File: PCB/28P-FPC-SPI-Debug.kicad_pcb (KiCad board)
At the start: 2 copper layers, 35.5 x 40 mm, 20 parts, among them J1 Conn_01x24, J3 SFV24R-1STBE1HLF, Q1 Si1308EDL

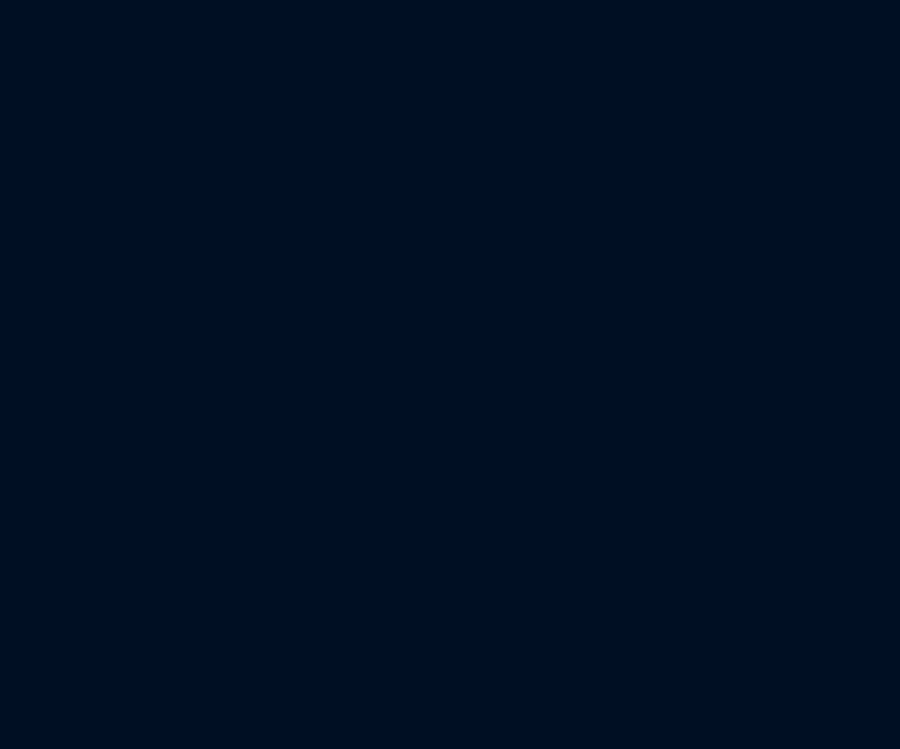
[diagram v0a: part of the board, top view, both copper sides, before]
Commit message: Modified power enable circuit to v2.2 ref design and added note.
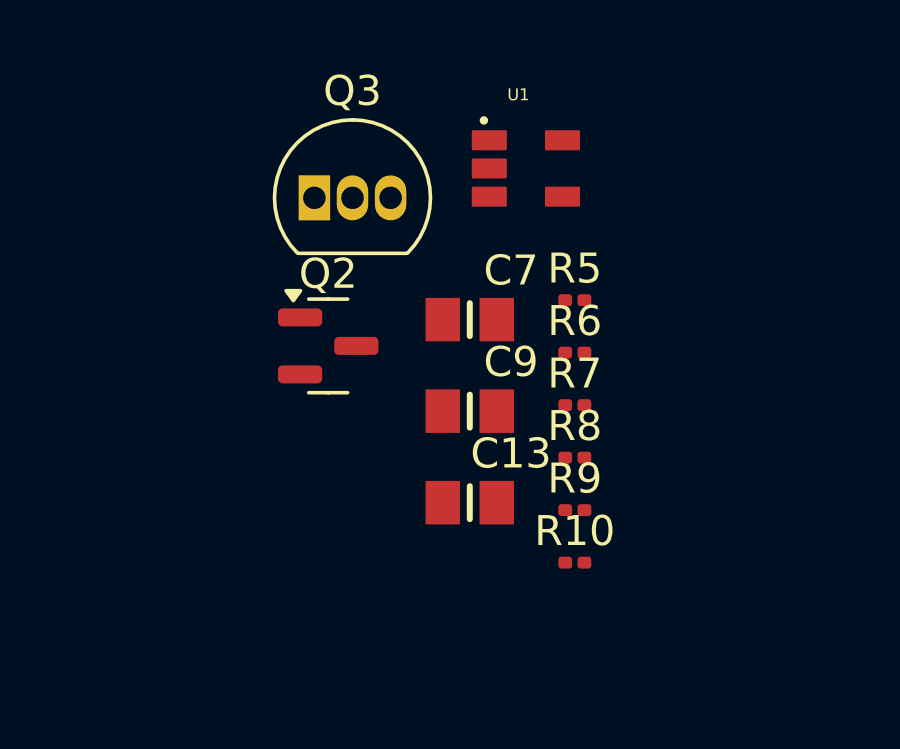
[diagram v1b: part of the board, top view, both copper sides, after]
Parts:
- added C13: 0.1u/50V, capacitors-cam:CAPC2012X140N, F.Cu at (96.2, 54.0)
- added C7: 1u/50V, capacitors-cam:CAPC2012X140N, F.Cu at (96.2, 47.9)
- added C9: 1u/50V, capacitors-cam:CAPC2012X140N, F.Cu at (96.2, 51.0)
- added Q2: AO3401A, Package_TO_SOT_SMD:SOT-23, F.Cu at (91.4, 48.8)
- added Q3: S8050, Package_TO_SOT_THT:TO-92_Inline, F.Cu at (91.0, 43.8)
- added R10: 100K, Resistor_SMD:R_0201_0603Metric, F.Cu at (99.7, 56.0)
- added R5: 1K, Resistor_SMD:R_0201_0603Metric, F.Cu at (99.7, 47.2)
- added R6: 47K, Resistor_SMD:R_0201_0603Metric, F.Cu at (99.7, 49.0)
- added R7: 47K, Resistor_SMD:R_0201_0603Metric, F.Cu at (99.7, 50.8)
- added R8: 1K, Resistor_SMD:R_0201_0603Metric, F.Cu at (99.7, 52.5)
- added R9: 47K, Resistor_SMD:R_0201_0603Metric, F.Cu at (99.7, 54.2)
- added U1: RT9193-33GB, VoltageRegulators:SOT94P279X129-5N, F.Cu at (98.0, 42.9)
- C3: value 1u/50V -> 0.1u/50V

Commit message: Added voltage level shifter TXB018PW
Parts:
- added J1: Conn_01x08, Connector_Samtec_HLE_THT:Samtec_HLE-104-02-xx-DV-TE_2x04_P2.54mm_Horizontal, F.Cu at (50.5, 47.9)
- moved R5 44.3 mm to (56.0, 54.5), turned to 180 degrees
- moved R8 43.8 mm to (56.0, 55.5)
- moved R7 43.2 mm to (56.6, 47.9), turned to 180 degrees
- moved R9 39.4 mm to (60.5, 59.0)
- moved R6 36.9 mm to (63.2, 54.5)
- moved Q2 30.1 mm to (63.0, 39.0)
- moved R10 28.4 mm to (71.3, 53.5)
- moved U1 25.0 mm to (75.0, 52.5)
- moved Q3 22.0 mm to (70.0, 37.5)
- moved C9 16.7 mm to (79.5, 49.5), turned to -90 degrees
- moved C13 14.9 mm to (82.0, 49.5), turned to -90 degrees
- moved Q1 13.0 mm to (128.5, 91.0)
- moved C7 11.8 mm to (84.5, 49.5), turned to -90 degrees
- moved L1 5.73 mm to (120.0, 82.5)
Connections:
- J3 pad 10: /RST -> /\RST
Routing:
- net Net-(Q3-B): track 0.00 -> 23.2 mm
- net Net-(U1-BP): track 0.00 -> 9.54 mm
- net /\RST: track 0.00 -> 6.62 mm
- net +3V3: track 0.00 -> 6.26 mm
- net /Vcc: track 0.00 -> 6.20 mm
- net /VCC_INT: track 0.00 -> 5.70 mm
- net GND: track 0.00 -> 3.29 mm
- net /VCC_EN: track 0.00 -> 2.14 mm
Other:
- board outline removed

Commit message: Added nets for TXB018PW. Resized PCB to size of 2.13in e-paper display with ~5mm excess on edges. Questionable part placement start.
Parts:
- removed the J1 at (93.0, 71.8)
- added C14: 1u/25V, capacitors-cam:CAPC1608X90N, F.Cu at (124.2, 29.5)
- added U2: TXB0108PW, Package_SO:TSSOP-20_4.4x6.5mm_P0.65mm, F.Cu at (163.0, 59.8)
- moved J1 145.3 mm to (195.0, 63.8), turned to 90 degrees
- moved R7 133.7 mm to (189.0, 66.0), turned to 0 degrees
- moved Q2 128.3 mm to (189.0, 63.0), turned to 90 degrees
- moved R5 126.7 mm to (182.3, 63.8), turned to 0 degrees
- moved R8 126.7 mm to (182.3, 64.8), turned to 180 degrees
- moved R9 124.0 mm to (184.3, 64.8), turned to 180 degrees
- moved Q3 123.9 mm to (188.6, 73.2), turned to 90 degrees
- moved R6 121.5 mm to (184.3, 63.8)
- moved R10 118.9 mm to (190.1, 57.8), turned to 90 degrees
- moved U1 114.2 mm to (189.1, 54.2), turned to 90 degrees
- moved C9 105.1 mm to (184.4, 55.4), turned to 0 degrees
- moved C13 102.4 mm to (184.4, 52.9), turned to 0 degrees
- moved C7 99.9 mm to (184.4, 50.4), turned to 0 degrees
- moved C12 76.3 mm to (179.6, 64.5), turned to -90 degrees
- moved J3 76.2 mm to (145.0, 60.0)
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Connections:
- J3 pad 10: /\RST -> /\EPD_RST
- J3 pad 11: /D/C -> /EPD_D/C
- J3 pad 12: /CS -> /EPD_CS
- J3 pad 13: /SCLK -> /EPD_SCLK
- J3 pad 14: /SDI -> /EPD_SDI
- J3 pad 9: /BUSY -> /EPD_BUSY
- R10 pad 1: GND -> /VCC_EN
- R10 pad 2: /VCC_EN -> GND
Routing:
- net Net-(Q3-B): track 23.2 -> 0.00 mm
- net Net-(Q2-G): track 0.00 -> 7.28 mm
- net /\RST: track 6.62 -> 0.00 mm
- net Net-(D2-A): track 0.00 -> 4.28 mm
- net Net-(D1-K): track 0.00 -> 4.20 mm
- net /Vcc: track 6.20 -> 9.92 mm
- net Net-(U1-BP): track 9.54 -> 5.84 mm
- net +3V3: track 6.26 -> 2.92 mm
- net /VDD: track 1.95 -> 0.00 mm
- net /VCC_INT: track 5.70 -> 7.59 mm
- net /D/C: track 1.07 -> 0.00 mm
- net /BUSY: track 1.07 -> 0.00 mm
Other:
- board outline added: 60 x 30 mm

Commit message: track placement, parts moved, nightmare fuel.
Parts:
- moved C14 49.8 mm to (167.0, 55.0), turned to 90 degrees
- moved C3 15.3 mm to (161.0, 69.4), turned to 90 degrees
- moved R5 12.3 mm to (191.2, 72.4), turned to -90 degrees
- moved C4 11.6 mm to (158.6, 69.4), turned to 90 degrees
- moved R8 11.1 mm to (190.0, 72.8)
- moved R6 9.96 mm to (190.0, 72.0)
- moved U2 9.44 mm to (172.3, 58.3)
- moved C5 8.83 mm to (156.6, 69.4), turned to 90 degrees
- moved R9 8.71 mm to (188.6, 72.4), turned to -90 degrees
- moved R2 7.45 mm to (172.3, 65.6), turned to 90 degrees
- moved D1 7.26 mm to (166.4, 72.2), turned to 180 degrees
- moved C2 6.91 mm to (153.0, 47.7), turned to -90 degrees
- moved C10 5.46 mm to (150.8, 69.4), turned to 90 degrees
- moved C1 4.86 mm to (151.0, 47.7), turned to -90 degrees
- moved R7 4.68 mm to (192.3, 62.6), turned to 90 degrees
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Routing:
- net /\RST: track 0.00 -> 43.5 mm, vias 0 -> 4
- net GND: track 3.29 -> 41.7 mm, vias 0 -> 7
- net /VCC_EN: track 2.14 -> 29.8 mm, vias 0 -> 3
- net /BUSY: track 0.00 -> 27.6 mm, vias 0 -> 2
- net +3V3: track 2.92 -> 27.4 mm, vias 0 -> 1
- net /SCLK: track 0.00 -> 24.3 mm, vias 0 -> 2
- net /D/C: track 0.00 -> 23.8 mm, vias 0 -> 2
- net /EPD_BUSY: track 0.00 -> 22.7 mm
- net /\EPD_RST: track 0.00 -> 22.6 mm
- net /EPD_D/C: track 0.00 -> 22.6 mm
- net /EPD_CS: track 0.00 -> 22.5 mm
- net /EPD_SCLK: track 0.00 -> 22.5 mm
- net /EPD_SDI: track 0.00 -> 22.4 mm
- net /SDI: track 0.00 -> 20.4 mm
- net /PREVGL: track 0.00 -> 20.2 mm, vias 0 -> 2
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
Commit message: track placement
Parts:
- moved R3 78.5 mm to (186.8, 49.4), turned to 90 degrees
- moved Q1 3.35 mm to (171.2, 64.8), turned to 90 degrees
- moved R2 2.10 mm to (173.2, 63.7)
- moved R1 2.07 mm to (168.2, 64.9)
- moved C11 2.01 mm to (170.4, 69.6)
- moved C12 1.05 mm to (179.4, 66.8)
- moved C6 0.22 mm to (154.4, 69.4)
- moved C8 0.22 mm to (152.8, 69.4)
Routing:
- net GND: track 41.7 -> 156.6 mm, vias 7 -> 14
- net +3V3: track 27.4 -> 91.5 mm, vias 1 -> 8
- net /GDR: track 2.03 -> 29.4 mm, vias 1 -> 3
- net /Vcc: track 16.6 -> 29.3 mm
- net Net-(D2-A): track 0.00 -> 11.7 mm
- net Net-(D1-K): track 0.00 -> 6.04 mm
- net /RESE: track 0.00 -> 2.08 mm

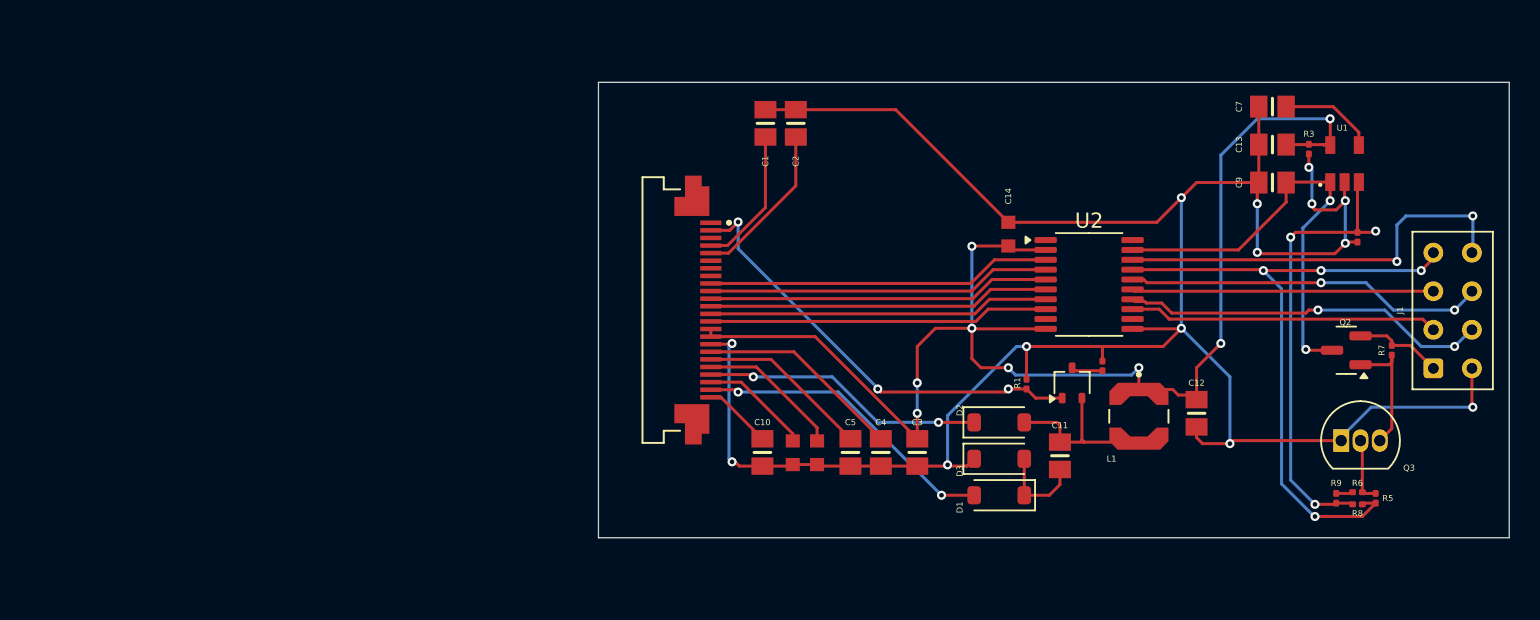
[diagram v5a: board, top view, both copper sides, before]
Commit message: Added breakout 28pin header for debugging. Track cleanup. Changed 0603 footprint due to clearance violations. Increased board size to fit header.
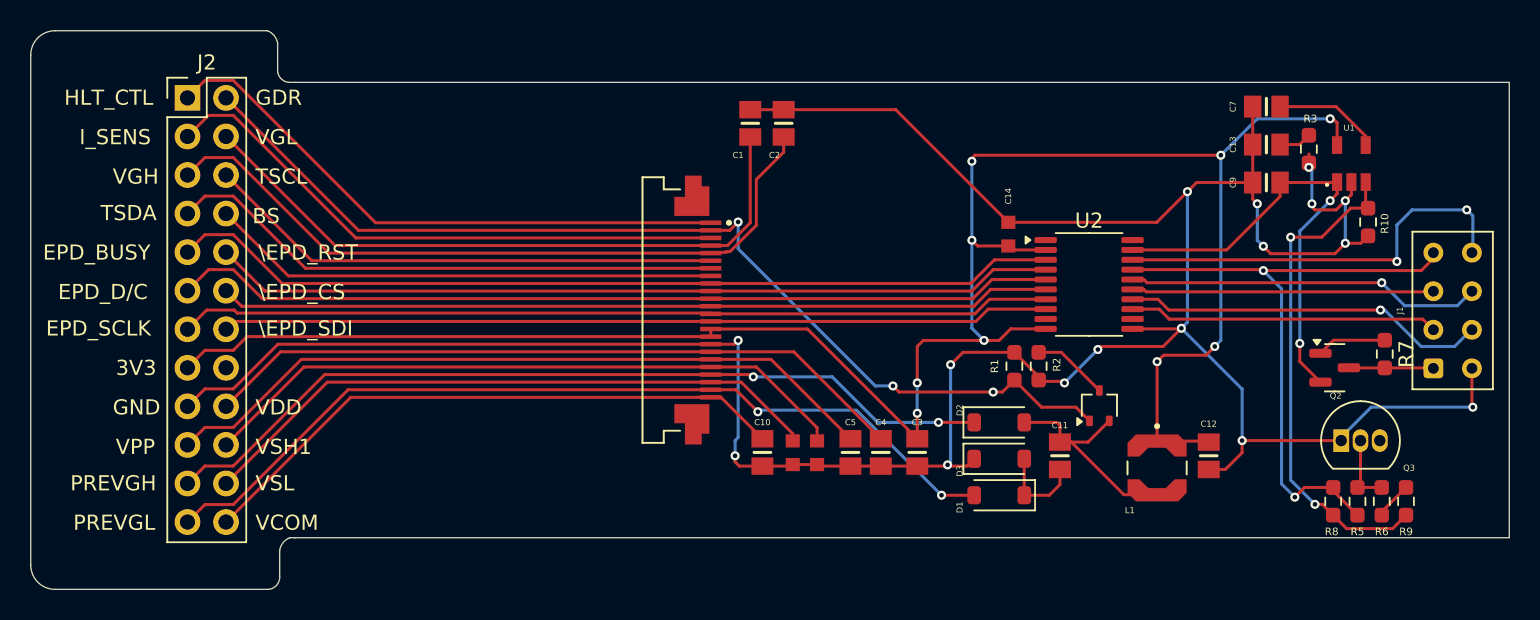
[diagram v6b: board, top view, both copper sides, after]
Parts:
- added J2: Conn_01x24, Connector_PinHeader_2.54mm:PinHeader_2x12_P2.54mm_Vertical, F.Cu at (112.9, 46.0)
- R1, R10, R2, R3, R6, R7, R8, R9: footprint Resistor_SMD:R_0201_0603Metric -> Resistor_SMD:R_0603_1608Metric_Pad0.98x0.95mm_HandSolder
- R5: value 1K -> 10K; footprint Resistor_SMD:R_0201_0603Metric -> Resistor_SMD:R_0603_1608Metric_Pad0.98x0.95mm_HandSolder
- moved R9 4.60 mm to (193.2, 72.6), turned to 90 degrees
- moved R2 4.20 mm to (169.0, 63.7), turned to -90 degrees
- moved L1 3.61 mm to (176.8, 70.4)
- moved C12 2.91 mm to (180.2, 69.6)
- moved Q1 2.34 mm to (173.0, 66.3)
- moved R6 1.71 mm to (191.6, 72.6), turned to 90 degrees
- moved R8 1.61 mm to (188.4, 72.6), turned to -90 degrees
- moved R1 1.43 mm to (167.4, 63.7)
- moved Q2 1.38 mm to (188.5, 63.8), turned to 0 degrees
- moved R10 1.22 mm to (190.7, 54.2)
- moved R5 1.22 mm to (190.0, 72.6)
- moved C1 1.00 mm to (150.0, 47.7)
- moved C2 0.80 mm to (152.2, 47.7)
- moved R7 0.53 mm to (191.8, 62.9), turned to -90 degrees
- moved U1 0.45 mm to (189.6, 50.4)
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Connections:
- Q2 pad 2: /VCC_INT -> /Vcc
- Q2 pad 3: /Vcc -> /VCC_INT
- R9 pad 1: Net-(R6-Pad1) -> /VCC_EN
- R9 pad 2: /VCC_EN -> Net-(R6-Pad1)
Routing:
- net +3V3: track 91.5 -> 139.2 mm, vias 8 -> 9
- net /HLT_CTL: track 0.00 -> 38.8 mm
- net GND: track 156.6 -> 195.1 mm, vias 14 -> 16
- net /GDR: track 29.4 -> 67.8 mm
- net /CURR_SENSE: track 0.00 -> 38.4 mm
- net /PREVGL: track 20.2 -> 58.4 mm
- net /PREVGH: track 18.7 -> 56.1 mm
- net /VGH: track 10.7 -> 47.9 mm
- net /TSDA: track 0.00 -> 36.9 mm
- net /VPP: track 11.4 -> 48.2 mm
- net /EPD_BUSY: track 22.7 -> 59.0 mm
- net /EPD_D/C: track 22.6 -> 58.4 mm
- net /VCOM: track 4.53 -> 39.9 mm
- net /EPD_SCLK: track 22.5 -> 57.6 mm
- net /VSL: track 7.06 -> 41.8 mm
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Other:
- board size 60 x 30 mm -> 97.4 x 36.8 mm
- board text added: "3V3"
- board text added: "BS"
- board text added: "EPD_BUSY"
- board text added: "EPD_D/C"
- board text added: "EPD_SCLK"
- board text added: "GDR"
- board text added: "GND"
- board text added: "HLT_CTL"
- board text added: "I_SENS"
- board text added: "PREVGH"
- board text added: "PREVGL"
- board text added: "TSCL"
- board text added: "TSDA"
- board text added: "VCOM"
- board text added: "VDD"
- board text added: "VGH"
- board text added: "VGL"
- board text added: "VPP"
- board text added: "VSH1"
- board text added: "VSL"
- board text added: "\EPD_CS"
- board text added: "\EPD_RST"
- board text added: "\EPD_SDI"

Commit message: Moved some parts. Cleared ERC errors and warnings. Ready?
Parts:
- moved R3 31.1 mm to (163.0, 69.4)
- moved R2 9.60 mm to (178.6, 64.0)
- moved R1 5.01 mm to (172.4, 64.0)
- moved C11 4.77 mm to (174.4, 72.2), turned to 0 degrees
- moved R11 4.50 mm to (186.2, 54.4), turned to 180 degrees
- moved U1 3.41 mm to (186.2, 50.6)
- moved Q1 3.36 mm to (175.4, 64.0)
- moved D1 3.20 mm to (169.6, 72.2)
- moved D2 3.20 mm to (169.6, 67.4)
- moved D3 3.20 mm to (169.6, 69.8)
- moved C13 2.20 mm to (181.8, 49.1)
- moved C7 2.20 mm to (181.8, 46.6)
- moved C9 2.20 mm to (181.8, 51.6)
- moved L1 1.80 mm to (176.8, 68.6), turned to 180 degrees
- moved Q2 1.48 mm to (187.1, 63.5), turned to 180 degrees
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- renumbered R7 to R10, R10 to R11, R8 to R6, R5 to R7, R6 to R8
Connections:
- Q2 pad 2: /Vcc -> /VCC_INT
- Q2 pad 3: /VCC_INT -> /Vcc
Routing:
- net GND: track 195.1 -> 204.9 mm, vias 16 -> 9
- net /Vcc: track 30.6 -> 24.3 mm, vias 2 -> 3
- net /PREVGL: track 58.4 -> 64.8 mm
- net /GDR: track 67.8 -> 73.8 mm, vias 3 -> 2
- net /VCC_EN: track 33.1 -> 27.6 mm
- net +3V3: track 139.2 -> 134.3 mm, vias 9 -> 8
- net /PREVGH: track 56.1 -> 59.4 mm
- net Net-(D2-A): track 15.2 -> 12.0 mm
- net Net-(Q2-G): track 4.59 -> 7.06 mm
- net /VCC_INT: track 5.58 -> 7.56 mm
- net /RESE: track 5.04 -> 3.19 mm
- net Net-(D1-K): track 6.04 -> 4.65 mm
- net /VGL: track 43.8 -> 45.0 mm
- net /SCLK: track 24.1 -> 23.2 mm
- net /VGH: track 47.9 -> 48.7 mm
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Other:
- outline, holes or cut-outs redrawn
- board text added: ">~< Rev0 PROTOTYPE"
